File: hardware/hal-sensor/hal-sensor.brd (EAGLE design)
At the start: 10 x 16.6 mm, 7 parts, among them IC1 DRV5023AJEDBZRQ1, Q1 BCX71SMD

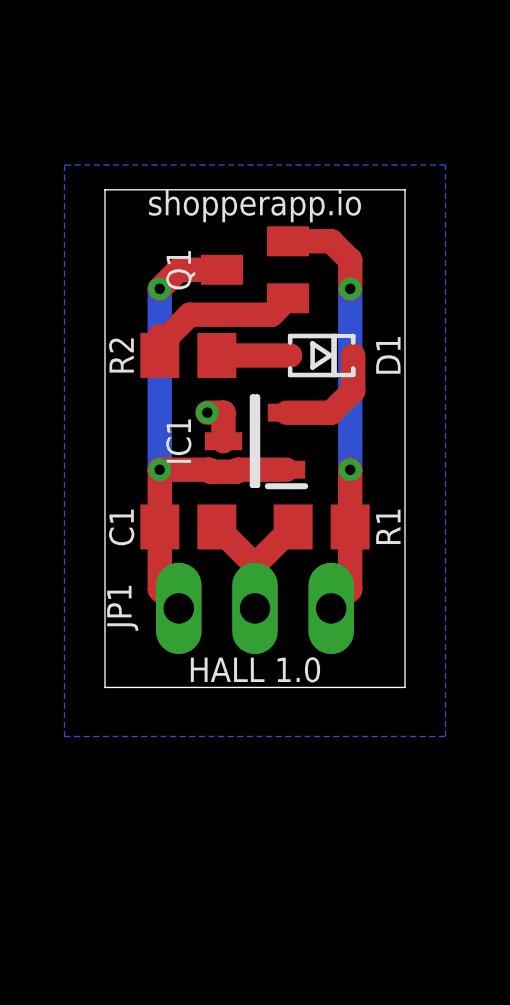
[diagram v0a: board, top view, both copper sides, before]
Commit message: redo hall sensor board
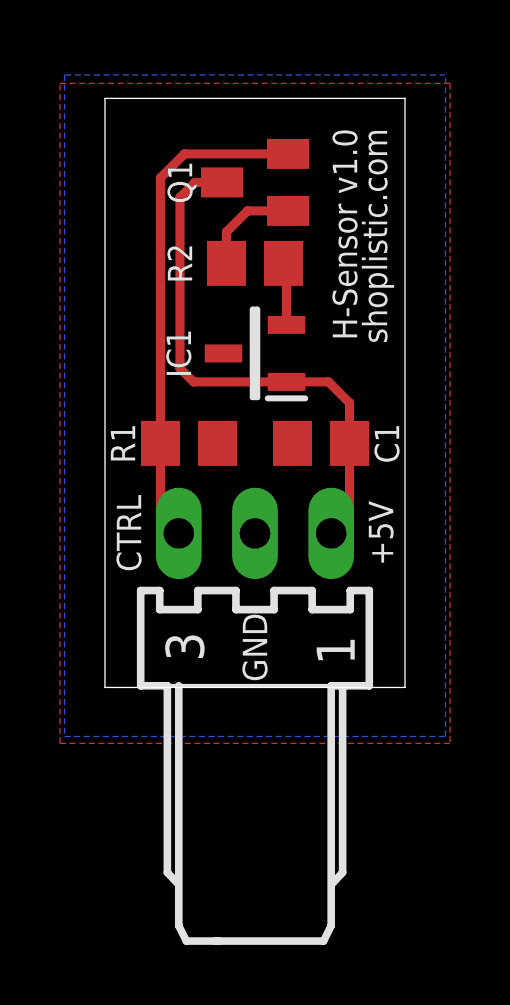
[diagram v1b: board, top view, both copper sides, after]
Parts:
- removed D1: (no value), BeagleBone_Black_Wireless:GHI-BASICCOMPONENTS_SOD323(NXP)REFLOW
- removed JP1: (no value), pinhead:1X03
- added J1: 22-05-7038-03, con-molex:7395-03
- moved C1 5.23 mm to (2.20, 8.50), turned to 180 degrees
- moved R1 5.23 mm to (-2.20, 8.50), turned to 0 degrees
- moved R2 3.79 mm to (0.00, 14.5)
- moved IC1 2.93 mm to (0.00, 11.5)
- moved Q1 2.91 mm to (0.00, 17.2)
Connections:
- removed net N$2: D1.A, R2.1
- net +5V: now also J1.1; no longer JP1.1
- net CTRL: now also J1.3; no longer JP1.3
- net GND: now also J1.2; no longer JP1.2
- net N$1: now also R2.1; no longer D1.C
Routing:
- net GND: track 6.53 -> 0.00 mm, vias 1 -> 0
- net CTRL: track 14.2 -> 16.7 mm, vias 2 -> 0
- net N$2: track 2.45 -> 0.00 mm
- net N$3: track 5.44 -> 3.39 mm
- net N$1: track 3.70 -> 2.09 mm
- net +5V: track 17.5 -> 18.0 mm, vias 2 -> 0
- added copper zone on layer 1, net GND
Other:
- board size 10 x 16.6 mm -> 10 x 19.6 mm
- board text added: "+5V"
- board text added: "CTRL"
- board text added: "GND"
- board text added: "H-Sensor v1.0"
- board text added: "shoplistic.com"
- board text removed: "HALL 1.0"
- board text removed: "shopperapp.io"

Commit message: tweak hal sensor board
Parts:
- moved Q1 0.50 mm to (0.00, 17.7)
- moved J1 0.10 mm to (0.00, 5.60)
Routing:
- net N$3: track 3.39 -> 3.89 mm
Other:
- board size 10 x 19.6 mm -> 10 x 20 mm
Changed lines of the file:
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@@
 <board>
 <plain>
-<wire x1="-5" y1="0.365" x2="5" y2="0.365" width="0" layer="20"/>
-<wire x1="5" y1="0.365" x2="5" y2="20" width="0" layer="20"/>
-<wire x1="5" y1="20" x2="-5" y2="20" width="0" layer="20"/>
-<wire x1="-5" y1="20" x2="-5" y2="0.365" width="0" layer="20"/>
-<text x="4" y="19" size="0.8128" layer="25" font="fixed" rot="R90" align="center-right">shoplistic.com</text>
-<text x="3" y="19" size="0.8128" layer="25" font="fixed" rot="R90" align="center-right">H-Sensor v1.0</text>
+<wire x1="-5" y1="0.5" x2="5" y2="0.5" width="0" layer="20"/>
+<wire x1="5" y1="0.5" x2="5" y2="20.5" width="0" layer="20"/>
+<wire x1="5" y1="20.5" x2="-5" y2="20.5" width="0" layer="20"/>
+<wire x1="-5" y1="20.5" x2="-5" y2="0.5" width="0" layer="20"/>
+<text x="4" y="20" size="0.8128" layer="25" font="fixed" rot="R90" align="center-right">shoplistic.com</text>
+<text x="3" y="20" size="0.8128" layer="25" font="fixed" rot="R90" align="center-right">H-Sensor v1.0</text>
 <text x="0" y="1.7" size="0.8128" layer="25" font="fixed" rot="R270" align="center">GND</text>
 <text x="4.2" y="5.5" size="0.8128" layer="25" font="fixed" rot="R90" align="center">+5V</text>
@@
 </autorouter>
 <elements>
-<element name="Q1" library="transistor-pnp" library_urn="urn:adsk.eagle:library:399" package="SOT23" package3d_urn="urn:adsk.eagle:package:28738/2" value="BCX71SMD" x="0" y="17.2" smashed="yes" rot="R90">
-<attribute name="NAME" x="-2.5" y="17.2" size="0.8128" layer="25" font="fixed" rot="R90" align="center"/>
+<element name="Q1" library="transistor-pnp" library_urn="urn:adsk.eagle:library:399" package="SOT23" package3d_urn="urn:adsk.eagle:package:28738/2" value="BCX71SMD" x="0" y="17.7" smashed="yes" rot="R90">
+<attribute name="NAME" x="-2.5" y="17.7" size="0.8128" layer="25" font="fixed" rot="R90" align="center"/>
 </element>
 <element name="R1" library="resistor" library_urn="urn:adsk.eagle:library:348" package="R0805" package3d_urn="urn:adsk.eagle:package:23553/2" value="10k" x="-2.2" y="8.5" smashed="yes">
@@
 <attribute name="NAME" x="-2.5" y="14.5" size="0.8128" layer="25" font="fixed" rot="R270" align="center"/>
 </element>
-<element name="J1" library="con-molex" library_urn="urn:adsk.eagle:library:165" package="7395-03" value="22-05-7038-03" x="0" y="5.5" smashed="yes">
-<attribute name="MF" value="MOLEX" x="0" y="5.5" size="1.778" layer="27" display="off"/>
-<attribute name="MPN" value="" x="0" y="5.5" size="1.778" layer="27" display="off"/>
-<attribute name="OC_FARNELL" value="unknown" x="0" y="5.5" size="1.778" layer="27" display="off"/>
-<attribute name="OC_NEWARK" value="unknown" x="0" y="5.5" size="1.778" layer="27" display="off"/>
+<element name="J1" library="con-molex" library_urn="urn:adsk.eagle:library:165" package="7395-03" value="22-05-7038-03" x="0" y="5.6" smashed="yes">
+<attribute name="MF" value="MOLEX" x="0" y="5.6" size="1.778" layer="27" display="off"/>
+<attribute name="MPN" value="" x="0" y="5.6" size="1.778" layer="27" display="off"/>
+<attribute name="OC_FARNELL" value="unknown" x="0" y="5.6" size="1.778" layer="27" display="off"/>
+<attribute name="OC_NEWARK" value="unknown" x="0" y="5.6" size="1.778" layer="27" display="off"/>
 </element>
 </elements>
@@
 <contactref element="C1" pad="1"/>
 <contactref element="J1" pad="1"/>
-<wire x1="3.15" y1="8.5" x2="3.15" y2="6.11" width="0.3048" layer="1"/>
-<wire x1="3.15" y1="6.11" x2="2.54" y2="5.5" width="0.3048" layer="1"/>
+<wire x1="3.15" y1="8.5" x2="3.15" y2="6.21" width="0.3048" layer="1"/>
+<wire x1="3.15" y1="6.21" x2="2.54" y2="5.6" width="0.3048" layer="1"/>
 <wire x1="-2.05" y1="10.55" x2="-2.5" y2="11" width="0.3048" layer="1"/>
 <wire x1="-2.05" y1="10.55" x2="1.05" y2="10.55" width="0.3048" layer="1"/>
@@
 <wire x1="2.45" y1="10.55" x2="1.05" y2="10.55" width="0.3048" layer="1"/>
 <wire x1="3.15" y1="9.85" x2="2.45" y2="10.55" width="0.3048" layer="1"/>
-<wire x1="-2" y1="17.2" x2="-1.1" y2="17.2" width="0.3048" layer="1"/>
-<wire x1="-2.5" y1="11" x2="-2.5" y2="16.7" width="0.3048" layer="1"/>
-<wire x1="-2.5" y1="16.7" x2="-2" y2="17.2" width="0.3048" layer="1"/>
+<wire x1="-2" y1="17.7" x2="-1.1" y2="17.7" width="0.3048" layer="1"/>
+<wire x1="-2.5" y1="11" x2="-2.5" y2="17.2" width="0.3048" layer="1"/>
+<wire x1="-2.5" y1="17.2" x2="-2" y2="17.7" width="0.3048" layer="1"/>
 </signal>
 <signal name="CTRL">
@@
 <contactref element="R1" pad="1"/>
 <contactref element="J1" pad="3"/>
-<wire x1="-2.35" y1="18.15" x2="1.1" y2="18.15" width="0.3048" layer="1"/>
-<wire x1="-3.15" y1="8.5" x2="-3.15" y2="6.11" width="0.3048" layer="1"/>
-<wire x1="-3.15" y1="6.11" x2="-2.54" y2="5.5" width="0.3048" layer="1"/>
-<wire x1="-3.15" y1="8.5" x2="-3.15" y2="17.35" width="0.3048" layer="1"/>
-<wire x1="-3.15" y1="17.35" x2="-2.35" y2="18.15" width="0.3048" layer="1"/>
+<wire x1="-2.35" y1="18.65" x2="1.1" y2="18.65" width="0.3048" layer="1"/>
+<wire x1="-3.15" y1="8.5" x2="-3.15" y2="6.21" width="0.3048" layer="1"/>
+<wire x1="-3.15" y1="6.21" x2="-2.54" y2="5.6" width="0.3048" layer="1"/>
+<wire x1="-3.15" y1="8.5" x2="-3.15" y2="17.85" width="0.3048" layer="1"/>
+<wire x1="-3.15" y1="17.85" x2="-2.35" y2="18.65" width="0.3048" layer="1"/>
 </signal>
 <signal name="GND">
@@
 <contactref element="C1" pad="2"/>
 <polygon width="0.3048" layer="16">
-<vertex x="-6.35" y="20.78"/>
+<vertex x="-6.35" y="21.28"/>
 <vertex x="-6.35" y="-1.27"/>
 <vertex x="6.35" y="-1.27"/>
-<vertex x="6.35" y="20.78"/>
+<vertex x="6.35" y="21.28"/>
 </polygon>
 <contactref element="J1" pad="2"/>
 <polygon width="0.3048" layer="1">
-<vertex x="-6.5" y="20.5"/>
-<vertex x="6.5" y="20.5"/>
+<vertex x="-6.5" y="21"/>
+<vertex x="6.5" y="21"/>
 <vertex x="6.5" y="-1.5"/>
 <vertex x="-6.5" y="-1.5"/>
@@
 <contactref element="R2" pad="2"/>
 <contactref element="Q1" pad="1"/>
-<wire x1="1.1" y1="16.25" x2="-0.25" y2="16.25" width="0.3048" layer="1"/>
-<wire x1="-0.95" y1="15.55" x2="-0.95" y2="14.5" width="0.3048" layer="1"/>
-<wire x1="-0.25" y1="16.25" x2="-0.95" y2="15.55" width="0.3048" layer="1"/>
+<wire x1="1.1" y1="16.75" x2="-0.25" y2="16.75" width="0.3048" layer="1"/>
+<wire x1="-0.95" y1="16.05" x2="-0.95" y2="14.5" width="0.3048" layer="1"/>
+<wire x1="-0.25" y1="16.75" x2="-0.95" y2="16.05" width="0.3048" layer="1"/>
 </signal>
 </signals>
